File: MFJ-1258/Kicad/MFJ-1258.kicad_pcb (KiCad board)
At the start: 2 copper layers, 77.8 x 54.3 mm, 19 parts, among them J1 C64-UserPort, J2 Screw_Terminal_01x01, J3 Screw_Terminal_01x01, Q1 2N3906, Q2 2N3906, Q3 2N3906, U1 NE555P

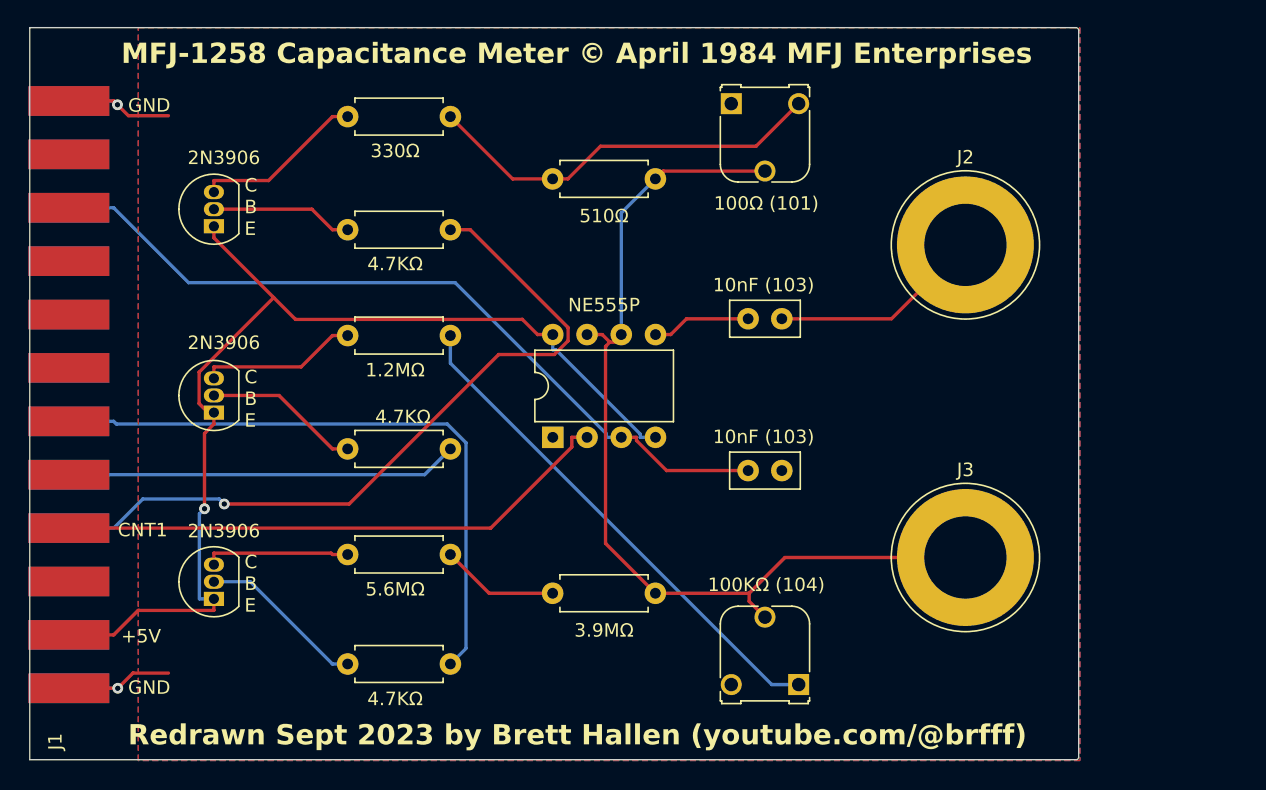
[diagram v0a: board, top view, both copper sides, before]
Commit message: Re-layout/Re-draw PCB
A few years more experience using KiCad now, updated from KiCad 6 to KiCad 9
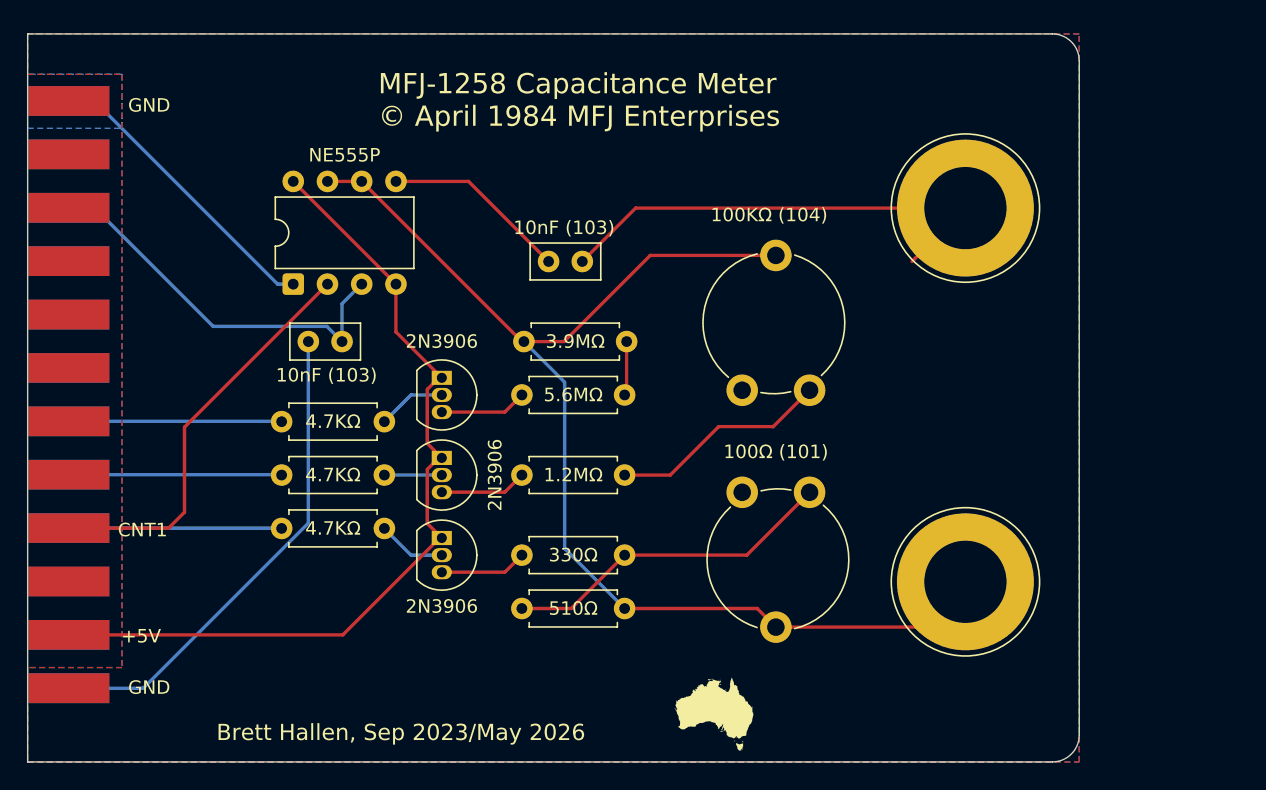
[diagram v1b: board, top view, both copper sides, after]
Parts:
- RV1, RV2: footprint Potentiometer_THT:Potentiometer_Runtron_RM-065_Vertical -> Potentiometer_THT:Potentiometer_Piher_PT-10-V10_Vertical
- moved C2 36.4 mm to (107.9, 93.4), turned to 0 degrees
- moved R8 35.0 mm to (131.3, 109.2)
- moved R1 31.9 mm to (131.3, 113.2)
- moved RV1 28.8 mm to (140.0, 104.6), turned to -90 degrees
- moved Q3 28.6 mm to (117.8, 108.0), turned to -90 degrees
- moved R3 25.4 mm to (105.9, 107.2), turned to 0 degrees
- moved Q1 23.5 mm to (117.8, 96.1), turned to -90 degrees
- moved U1 22.4 mm to (106.7, 89.1)
- moved R5 21.9 mm to (105.9, 99.3), turned to 0 degrees
- moved RV2 21.8 mm to (145.0, 97.0), turned to 90 degrees
- moved R7 21.1 mm to (123.9, 93.4), turned to 0 degrees
- moved R6 17.5 mm to (131.3, 97.3)
- moved Q2 17.2 mm to (117.8, 102.0), turned to -90 degrees
- moved R2 16.6 mm to (131.3, 103.3)
- moved C1 15.4 mm to (128.2, 87.4)
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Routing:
- net /PB1: track 55.8 -> 15.8 mm, vias 1 -> 0
- net /GND: track 23.2 -> 58.6 mm, vias 2 -> 0
- net /PB3: track 47.0 -> 15.8 mm
- net /PB7: track 58.8 -> 29.2 mm
- net Net-(R2-Pad1): track 37.8 -> 16.3 mm
- net Net-(J3-Pin_1): track 70.9 -> 91.6 mm
- net Net-(J2-Pin_1): track 15.9 -> 35.7 mm
- net /+5V: track 79.9 -> 63.7 mm, vias 1 -> 0
- net /PB2: track 29.1 -> 15.8 mm
- net /CNT1: track 41.6 -> 30.4 mm
- net Net-(Q1-B): track 12.4 -> 5.08 mm
- net Net-(Q2-B): track 11.6 -> 4.26 mm
- net Net-(U1-CV): track 7.35 -> 13.8 mm
- net Net-(Q3-C): track 12.7 -> 6.47 mm
- net Net-(Q3-B): track 10.6 -> 5.08 mm
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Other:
- board size 77.8 x 54.3 mm -> 78 x 54 mm
- board text added: "Brett Hallen, Sep 2023/May 2026"
- board text removed: "C B E"
- board text removed: "Redrawn Sept 2023 by Brett Hallen (youtube.com/@brfff)"
